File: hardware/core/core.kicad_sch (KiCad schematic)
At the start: 99 parts, among them J1 9V_IN, J2 MIDI IN, J3 MIDI OUT 1, J4 SWITCHES OUT, J5 EXP/AUX IN, J7 LCD, J8 USB_C_Receptacle_USB2.0_16P, J9 MIDI OUT 2/3, K1 G5V-1, K2 G5V-1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

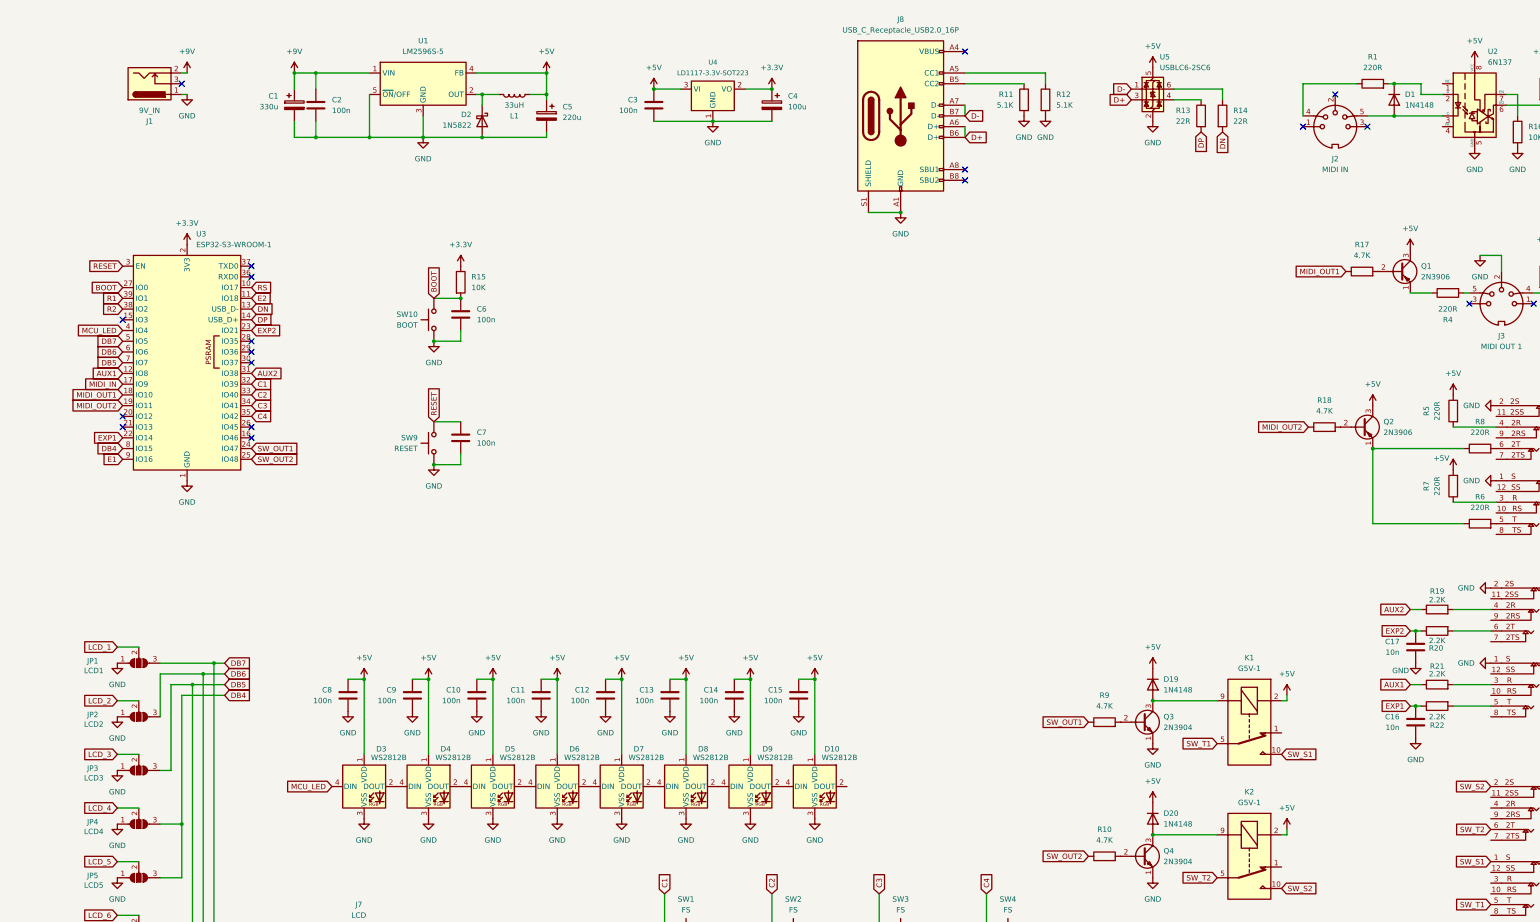
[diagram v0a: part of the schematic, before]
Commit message: Update PCB layout with revised nets and add D21 WS2812B LED
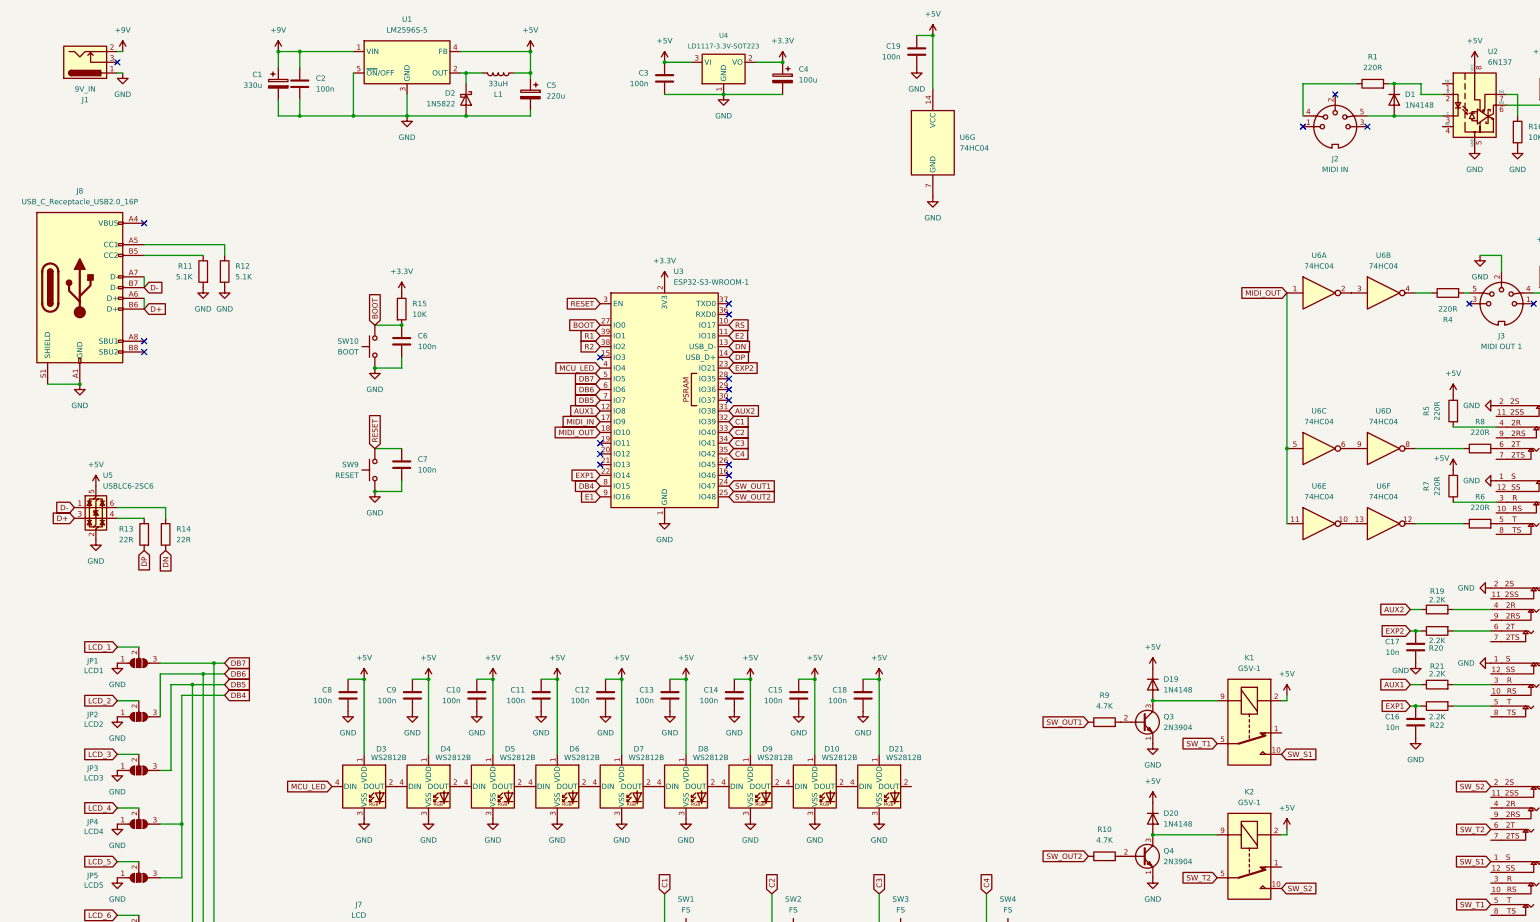
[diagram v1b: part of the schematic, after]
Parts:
- removed Q1, Q2: 2N3906, Package_TO_SOT_THT:TO-92_Inline_Wide, symbol Transistor_BJT:2N3906
- removed R17, R18: 4.7K, Resistor_THT:R_Axial_DIN0204_L3.6mm_D1.6mm_P7.62mm_Horizontal, symbol Device:R
- added C18, C19: 100n, Capacitor_THT:C_Rect_L7.0mm_W2.5mm_P5.00mm, symbol Device:C
- added D21: WS2812B, midilord:APA106, symbol LED:WS2812B
- added U6: 74HC04, Package_DIP:DIP-14_W7.62mm_Socket_LongPads, symbol 74xx:74HC04
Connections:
- net +5V: now also C18.1, C19.1, D21.1 (VDD), U6.14 (VCC)
- net GND: now also C18.2, C19.2, D21.3 (VSS), U6.7 (GND)
- net at D10.2 (DOUT): now also D21.4 (DIN)
- net at R6.1: now also U6.12; no longer R8.1
- net at R4.1: now also U6.4
- net MIDI_OUT1 renamed MIDI_OUT
- net MIDI_OUT: now also U6.1, U6.11, U6.5
- net MIDI_OUT2: no longer names the net of U3.19 (IO11)
- new net: U6.2, U6.3
- new net: R8.1, U6.8
- new net: U6.6, U6.9
- new net: U6.10, U6.13
- no-connect marks 19 -> 20
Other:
- moved on the sheet: C1, C2, C3, C4, C5, C6, C7, D2, J1, J8, L1, R11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

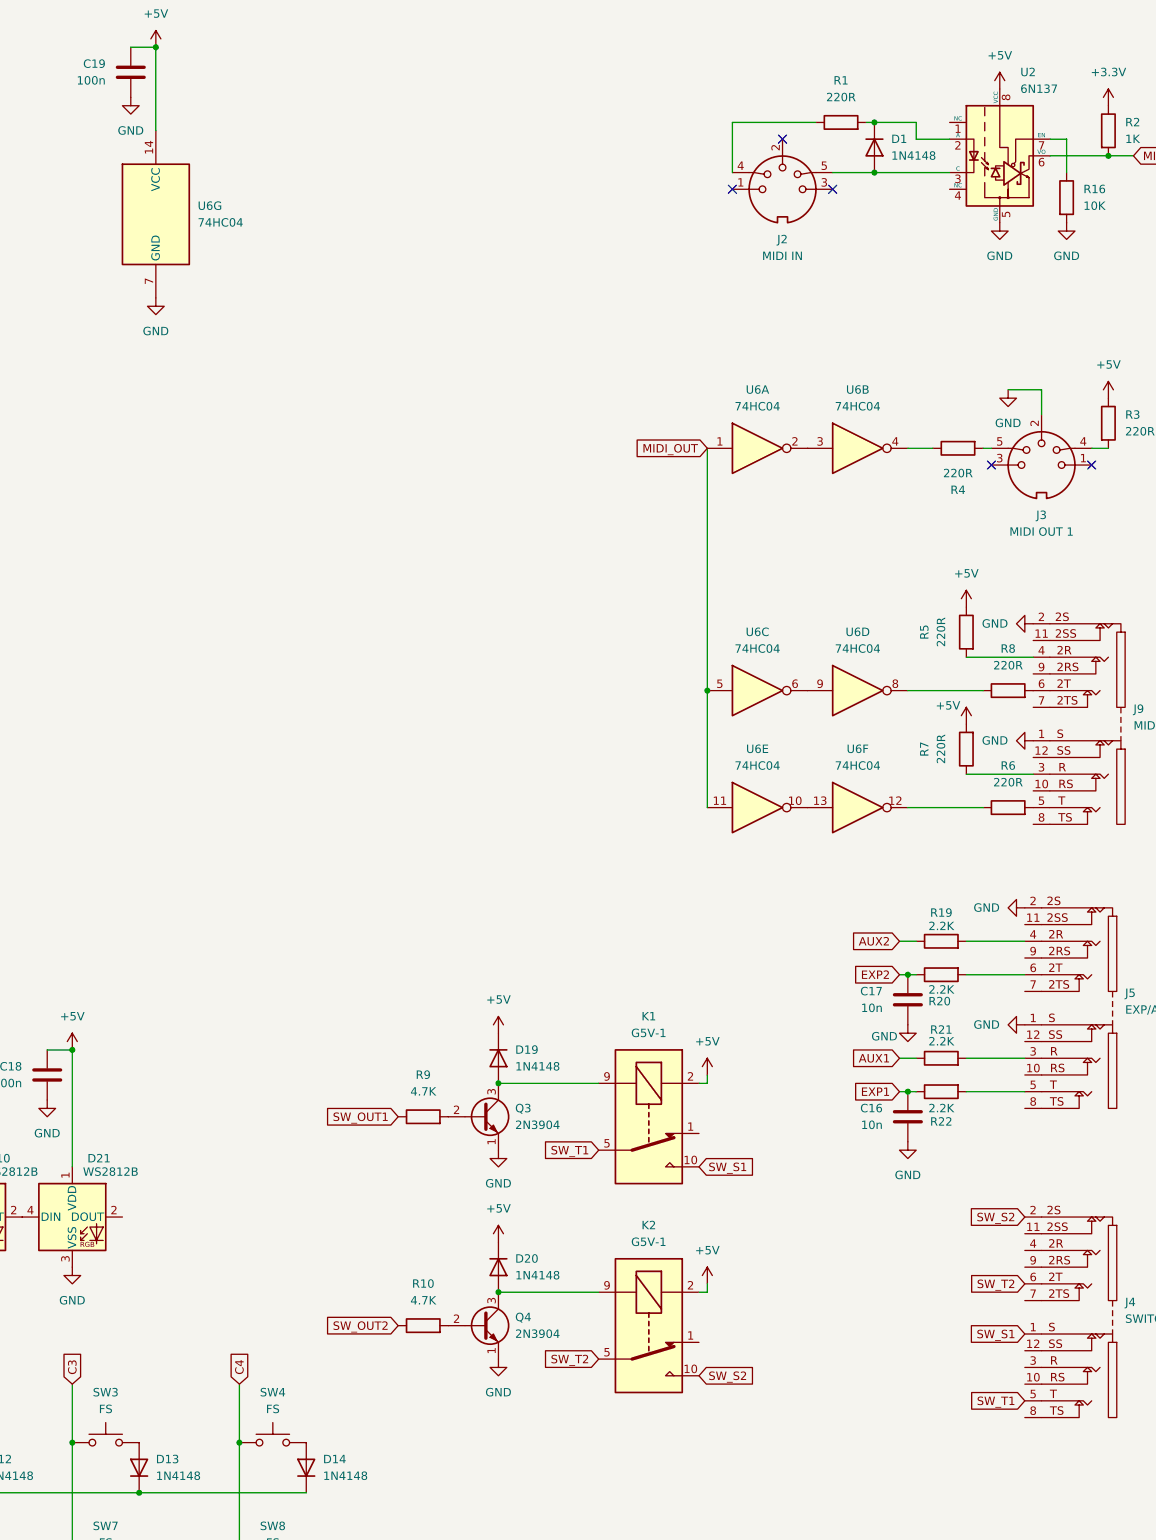
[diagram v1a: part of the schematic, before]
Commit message: Update PCB layout and fix DRC warnings for unconnected pins
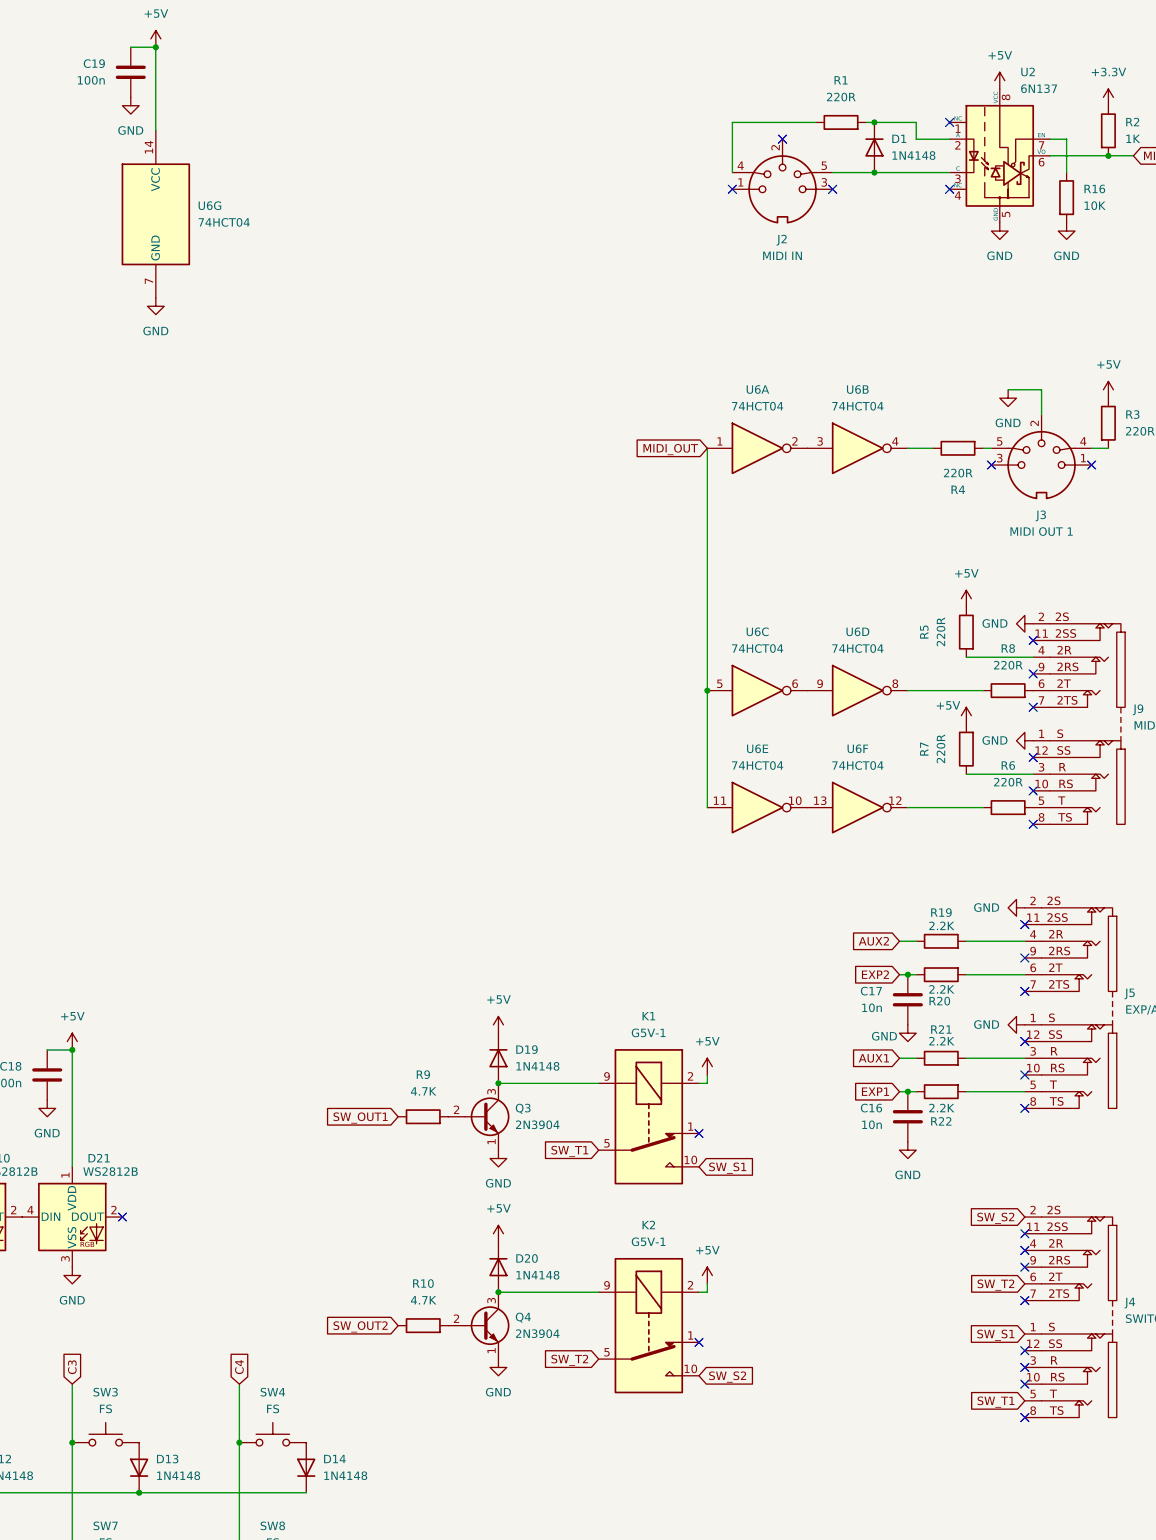
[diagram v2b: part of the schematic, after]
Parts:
- U6: value 74HC04 -> 74HCT04; symbol 74xx:74HC04 -> 74xx:74AHCT04
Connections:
- no-connect marks 20 -> 45
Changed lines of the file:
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@@
 	)
 	(no_connect
+		(at 368.3 182.88)
+	)
+	(no_connect
+		(at 368.3 212.09)
+	)
+	(no_connect
+		(at 368.3 224.79)
+	)
+	(no_connect
+		(at 368.3 160.02)
+	)
+	(no_connect
+		(at 369.57 139.7)
+	)
+	(no_connect
+		(at 318.77 191.77)
+	)
+	(no_connect
+		(at 368.3 170.18)
+	)
+	(no_connect
 		(at 323.85 48.26)
 	)
 	(no_connect
+		(at 368.3 177.8)
+	)
+	(no_connect
+		(at 369.57 121.92)
+	)
+	(no_connect
+		(at 231.14 204.47)
+	)
+	(no_connect
 		(at 187.96 90.17)
 	)
 	(no_connect
+		(at 356.87 48.26)
+	)
+	(no_connect
 		(at 49.53 99.06)
 	)
@@
 	)
 	(no_connect
+		(at 318.77 223.52)
+	)
+	(no_connect
 		(at 49.53 101.6)
 	)
 	(no_connect
+		(at 368.3 207.01)
+	)
+	(no_connect
+		(at 369.57 144.78)
+	)
+	(no_connect
 		(at 339.09 48.26)
 	)
@@
 	)
 	(no_connect
+		(at 369.57 116.84)
+	)
+	(no_connect
+		(at 368.3 227.33)
+	)
+	(no_connect
+		(at 369.57 127)
+	)
+	(no_connect
 		(at 43.18 33.02)
 	)
 	(no_connect
+		(at 368.3 234.95)
+	)
+	(no_connect
 		(at 378.46 90.17)
 	)
 	(no_connect
+		(at 368.3 187.96)
+	)
+	(no_connect
 		(at 331.47 40.64)
 	)
 	(no_connect
+		(at 356.87 38.1)
+	)
+	(no_connect
+		(at 368.3 217.17)
+	)
+	(no_connect
 		(at 187.96 113.03)
 	)
 	(no_connect
+		(at 369.57 134.62)
+	)
+	(no_connect
 		(at 157.48 123.19)
 	)
+	(no_connect
+		(at 368.3 165.1)
+	)
+	(no_connect
+		(at 368.3 229.87)
+	)
+	(no_connect
+		(at 368.3 209.55)
+	)
 	(wire
 		(pts
@@
 	)
 	(symbol
-		(lib_id "74xx:74HC04")
+		(lib_id "74xx:74AHCT04")
 		(at 236.22 52.07 0)
 		(unit 7)
@@
 			)
 		)
-		(property "Value" "74HC04"
+		(property "Value" "74HCT04"
 			(at 242.57 53.3399 0)
 			(effects
@@
 			)
 		)
-		(property "Datasheet" "https://assets.nexperia.com/documents/data-sheet/74HC_HCT04.pdf"
+		(property "Datasheet" "https://assets.nexperia.com/documents/data-sheet/74AHC_AHCT04.pdf"
 			(at 236.22 52.07 0)
 			(effects
@@
 	)
 	(symbol
-		(lib_id "74xx:74HC04")
+		(lib_id "74xx:74AHCT04")
 		(at 342.9 87.63 0)
 		(unit 2)
@@
 			)
 		)
-		(property "Value" "74HC04"
+		(property "Value" "74HCT04"
 			(at 342.9 81.28 0)
 			(effects
@@
 			)
 		)
-		(property "Datasheet" "https://assets.nexperia.com/documents/data-sheet/74HC_HCT04.pdf"
+		(property "Datasheet" "https://assets.nexperia.com/documents/data-sheet/74AHC_AHCT04.pdf"
 			(at 342.9 87.63 0)
 			(effects
@@
 	)
 	(symbol
-		(lib_id "74xx:74HC04")
+		(lib_id "74xx:74AHCT04")
 		(at 342.9 124.46 0)
 		(unit 4)
@@
 			)
 		)
-		(property "Value" "74HC04"
+		(property "Value" "74HCT04"
 			(at 342.9 118.11 0)
 			(effects
@@
 			)
 		)
-		(property "Datasheet" "https://assets.nexperia.com/documents/data-sheet/74HC_HCT04.pdf"
+		(property "Datasheet" "https://assets.nexperia.com/documents/data-sheet/74AHC_AHCT04.pdf"
 			(at 342.9 124.46 0)
 			(effects
@@
 	)
 	(symbol
-		(lib_id "74xx:74HC04")
+		(lib_id "74xx:74AHCT04")
 		(at 342.9 142.24 0)
 		(unit 6)
@@
 			)
 		)
-		(property "Value" "74HC04"
+		(property "Value" "74HCT04"
 			(at 342.9 135.89 0)
 			(effects
@@
 			)
 		)
-		(property "Datasheet" "https://assets.nexperia.com/documents/data-sheet/74HC_HCT04.pdf"
+		(property "Datasheet" "https://assets.nexperia.com/documents/data-sheet/74AHC_AHCT04.pdf"
 			(at 342.9 142.24 0)
 			(effects
@@
 	)
 	(symbol
-		(lib_id "74xx:74HC04")
+		(lib_id "74xx:74AHCT04")
 		(at 327.66 87.63 0)
 		(unit 1)
@@
 			)
 		)
-		(property "Value" "74HC04"
+		(property "Value" "74HCT04"
 			(at 327.66 81.28 0)
 			(effects
@@
 			)
 		)
-		(property "Datasheet" "https://assets.nexperia.com/documents/data-sheet/74HC_HCT04.pdf"
+		(property "Datasheet" "https://assets.nexperia.com/documents/data-sheet/74AHC_AHCT04.pdf"
 			(at 327.66 87.63 0)
 			(effects
@@
 	)
 	(symbol
-		(lib_id "74xx:74HC04")
+		(lib_id "74xx:74AHCT04")
 		(at 327.66 124.46 0)
 		(unit 3)
@@
 			)
 		)
-		(property "Value" "74HC04"
+		(property "Value" "74HCT04"
 			(at 327.66 118.11 0)
 			(effects
@@
 			)
 		)
-		(property "Datasheet" "https://assets.nexperia.com/documents/data-sheet/74HC_HCT04.pdf"
+		(property "Datasheet" "https://assets.nexperia.com/documents/data-sheet/74AHC_AHCT04.pdf"
 			(at 327.66 124.46 0)
 			(effects
@@
 	)
 	(symbol
-		(lib_id "74xx:74HC04")
+		(lib_id "74xx:74AHCT04")
 		(at 327.66 142.24 0)
 		(unit 5)
@@
 			)
 		)
-		(property "Value" "74HC04"
+		(property "Value" "74HCT04"
 			(at 327.66 135.89 0)
 			(effects
@@
 			)
 		)
-		(property "Datasheet" "https://assets.nexperia.com/documents/data-sheet/74HC_HCT04.pdf"
+		(property "Datasheet" "https://assets.nexperia.com/documents/data-sheet/74AHC_AHCT04.pdf"
 			(at 327.66 142.24 0)
 			(effects
